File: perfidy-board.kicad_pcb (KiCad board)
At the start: 4 copper layers, 70.6 x 60.5 mm, 572 parts

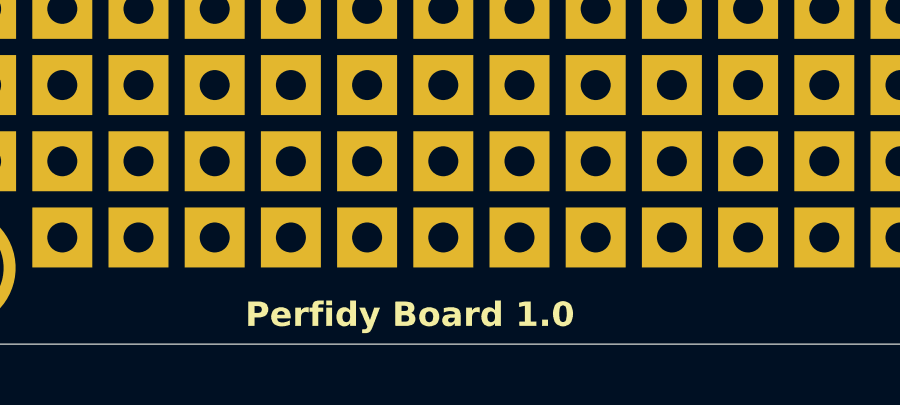
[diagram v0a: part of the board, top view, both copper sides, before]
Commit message: v1.1 changes mid layers to hidden text
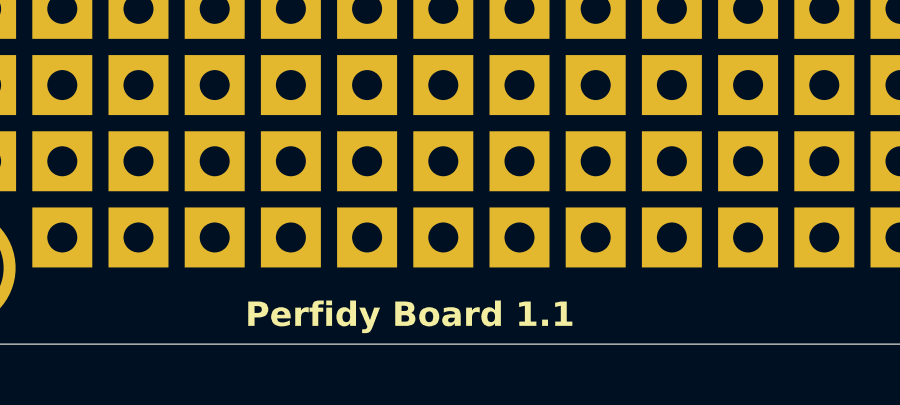
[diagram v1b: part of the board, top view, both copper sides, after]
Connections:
- TP108 pad 1: unconnected-(TP108-Pad1) -> /A
- TP115 pad 1: unconnected-(TP115-Pad1) -> /B
- TP116 pad 1: /F -> /B
- TP12 pad 1: /F -> unconnected-(TP12-Pad1)
- TP120 pad 1: unconnected-(TP120-Pad1) -> /D
- TP126 pad 1: unconnected-(TP126-Pad1) -> /I
- TP127 pad 1: unconnected-(TP127-Pad1) -> /F
- TP140 pad 1: unconnected-(TP140-Pad1) -> /B
- TP141 pad 1: /F -> unconnected-(TP141-Pad1)
- TP143 pad 1: unconnected-(TP143-Pad1) -> /B
- TP165 pad 1: unconnected-(TP165-Pad1) -> /B
- TP168 pad 1: /F -> unconnected-(TP168-Pad1)
- TP170 pad 1: unconnected-(TP170-Pad1) -> /C
- TP191 pad 1: unconnected-(TP191-Pad1) -> /B
- TP196 pad 1: unconnected-(TP196-Pad1) -> /C
- TP209 pad 1: /A -> unconnected-(TP209-Pad1)
- TP217 pad 1: unconnected-(TP217-Pad1) -> /B
- TP222 pad 1: unconnected-(TP222-Pad1) -> /C
- TP230 pad 1: unconnected-(TP230-Pad1) -> /I
- TP231 pad 1: unconnected-(TP231-Pad1) -> /F
- TP243 pad 1: unconnected-(TP243-Pad1) -> /B
- TP248 pad 1: unconnected-(TP248-Pad1) -> /C
- TP270 pad 1: unconnected-(TP270-Pad1) -> /B
- TP273 pad 1: unconnected-(TP273-Pad1) -> /C
- TP274 pad 1: /B -> unconnected-(TP274-Pad1)
- TP282 pad 1: unconnected-(TP282-Pad1) -> /H
- TP283 pad 1: unconnected-(TP283-Pad1) -> /E
- TP293 pad 1: unconnected-(TP293-Pad1) -> /A
- TP297 pad 1: unconnected-(TP297-Pad1) -> /C
- TP298 pad 1: unconnected-(TP298-Pad1) -> /C
- TP305 pad 1: unconnected-(TP305-Pad1) -> /D
- TP308 pad 1: unconnected-(TP308-Pad1) -> /E
- TP309 pad 1: unconnected-(TP309-Pad1) -> /H
- TP331 pad 1: /C -> unconnected-(TP331-Pad1)
- TP343 pad 1: /A -> unconnected-(TP343-Pad1)
- TP372 pad 1: /B -> unconnected-(TP372-Pad1)
- TP394 pad 1: unconnected-(TP394-Pad1) -> /G
- TP403 pad 1: /E -> unconnected-(TP403-Pad1)
- TP413 pad 1: unconnected-(TP413-Pad1) -> /G
- TP478 pad 1: /B -> unconnected-(TP478-Pad1)
- TP491 pad 1: /C -> unconnected-(TP491-Pad1)
- TP51 pad 1: /E -> unconnected-(TP51-Pad1)
- TP566 pad 1: /D -> unconnected-(TP566-Pad1)
- TP567 pad 1: /D -> unconnected-(TP567-Pad1)
- TP568 pad 1: /D -> unconnected-(TP568-Pad1)
- TP569 pad 1: /D -> unconnected-(TP569-Pad1)
- TP571 pad 1: /D -> unconnected-(TP571-Pad1)
- TP69 pad 1: /B -> unconnected-(TP69-Pad1)
- TP89 pad 1: /F -> unconnected-(TP89-Pad1)
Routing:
- net /E: track 64.0 -> 3.59 mm
- net /G: track 0.00 -> 49.3 mm
- net /B: track 62.6 -> 24.5 mm
- net /D: track 13.9 -> 28.5 mm
- net /I: track 0.00 -> 11.0 mm
- net /F: track 19.4 -> 11.0 mm
- net /C: track 23.4 -> 17.3 mm
- net /A: track 20.8 -> 26.1 mm
- net /H: track 0.00 -> 3.59 mm
